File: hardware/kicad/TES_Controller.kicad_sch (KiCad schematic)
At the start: 84 parts, among them CN1 B2PS-VH(LF)(SN), CN2 S4B-XH-A(LF)(SN), CN3 DG381-3.5-02P-14-00A(H), CN5 DG381-3.5-02P-14-00A(H), CN6 DG381-3.5-02P-14-00A(H), Q1 AO3400A, Q2 AO3400A, Q3 AO3400A, Q4 AO3401A, U1 ESP32-S3-WROOM-1-N16R8, U10 DG301-5.0-02P-14-00A(H), U12 TJA1051T/3/1J, U13 24C02S, U5 ADS1115IDGSR, U6 AMS1117-3.3, U8 LMZM23601V5SILR

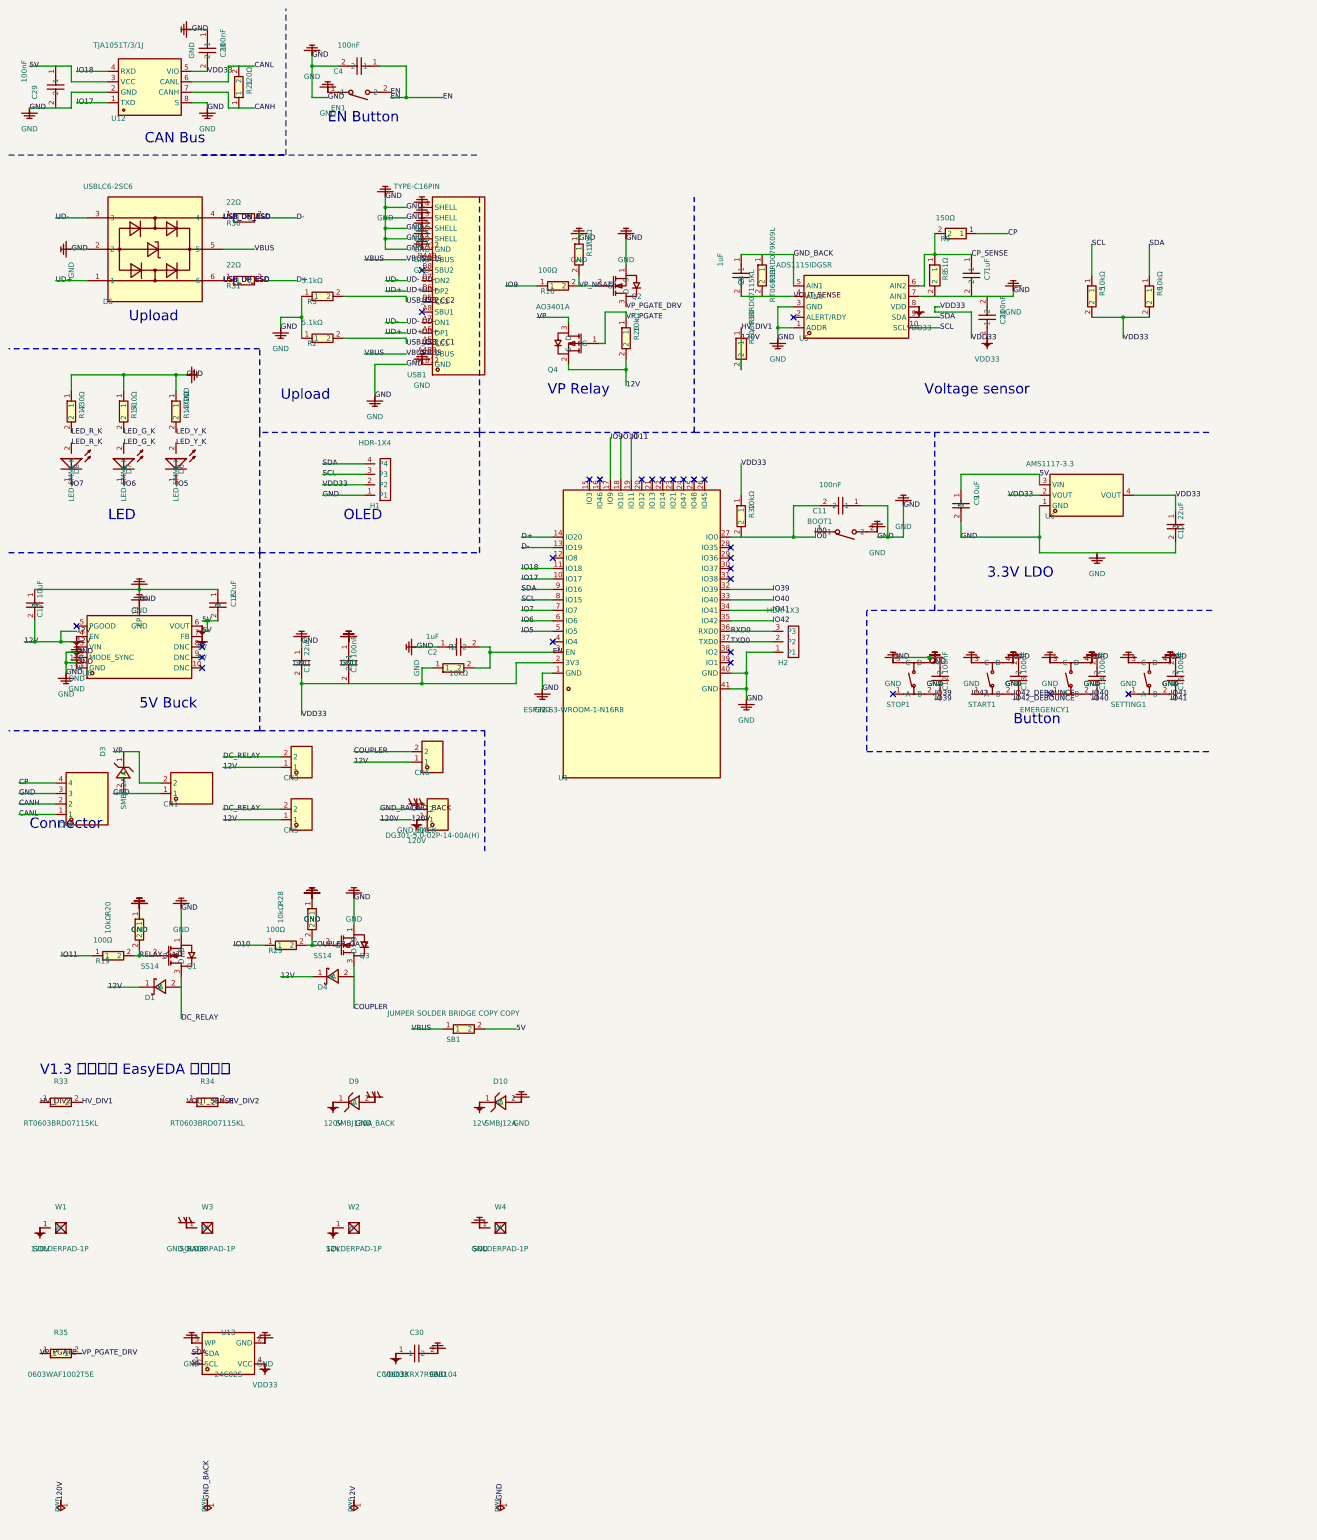
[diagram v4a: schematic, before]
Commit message: Identify the board revision with a divider on ADS1115 AIN3
The U13 EEPROM could not be placed: SDA, SCL and VCC all had to reach it,
and the nearest free spot was 32 mm from the I2C pins. AIN3 was tied to
ground and only served as the CP measurement's negative input, so it now
carries HW_ID from R36/R37 (10k/10k = level 6 = V1.3). Old boards read
0 V and keep the 30.000 coefficient; one net reaches U5 instead of three.

Schematic 236/236 zero difference, ERC 0. PCB hand-routed on the top
layer, DRC 0 errors / 0 unconnected, warnings unchanged at 182,
mechanical lock untouched. R35 and D10 are still to be applied.

Co-Authored-By: Claude Opus 5.5 <noreply@anthropic.com>
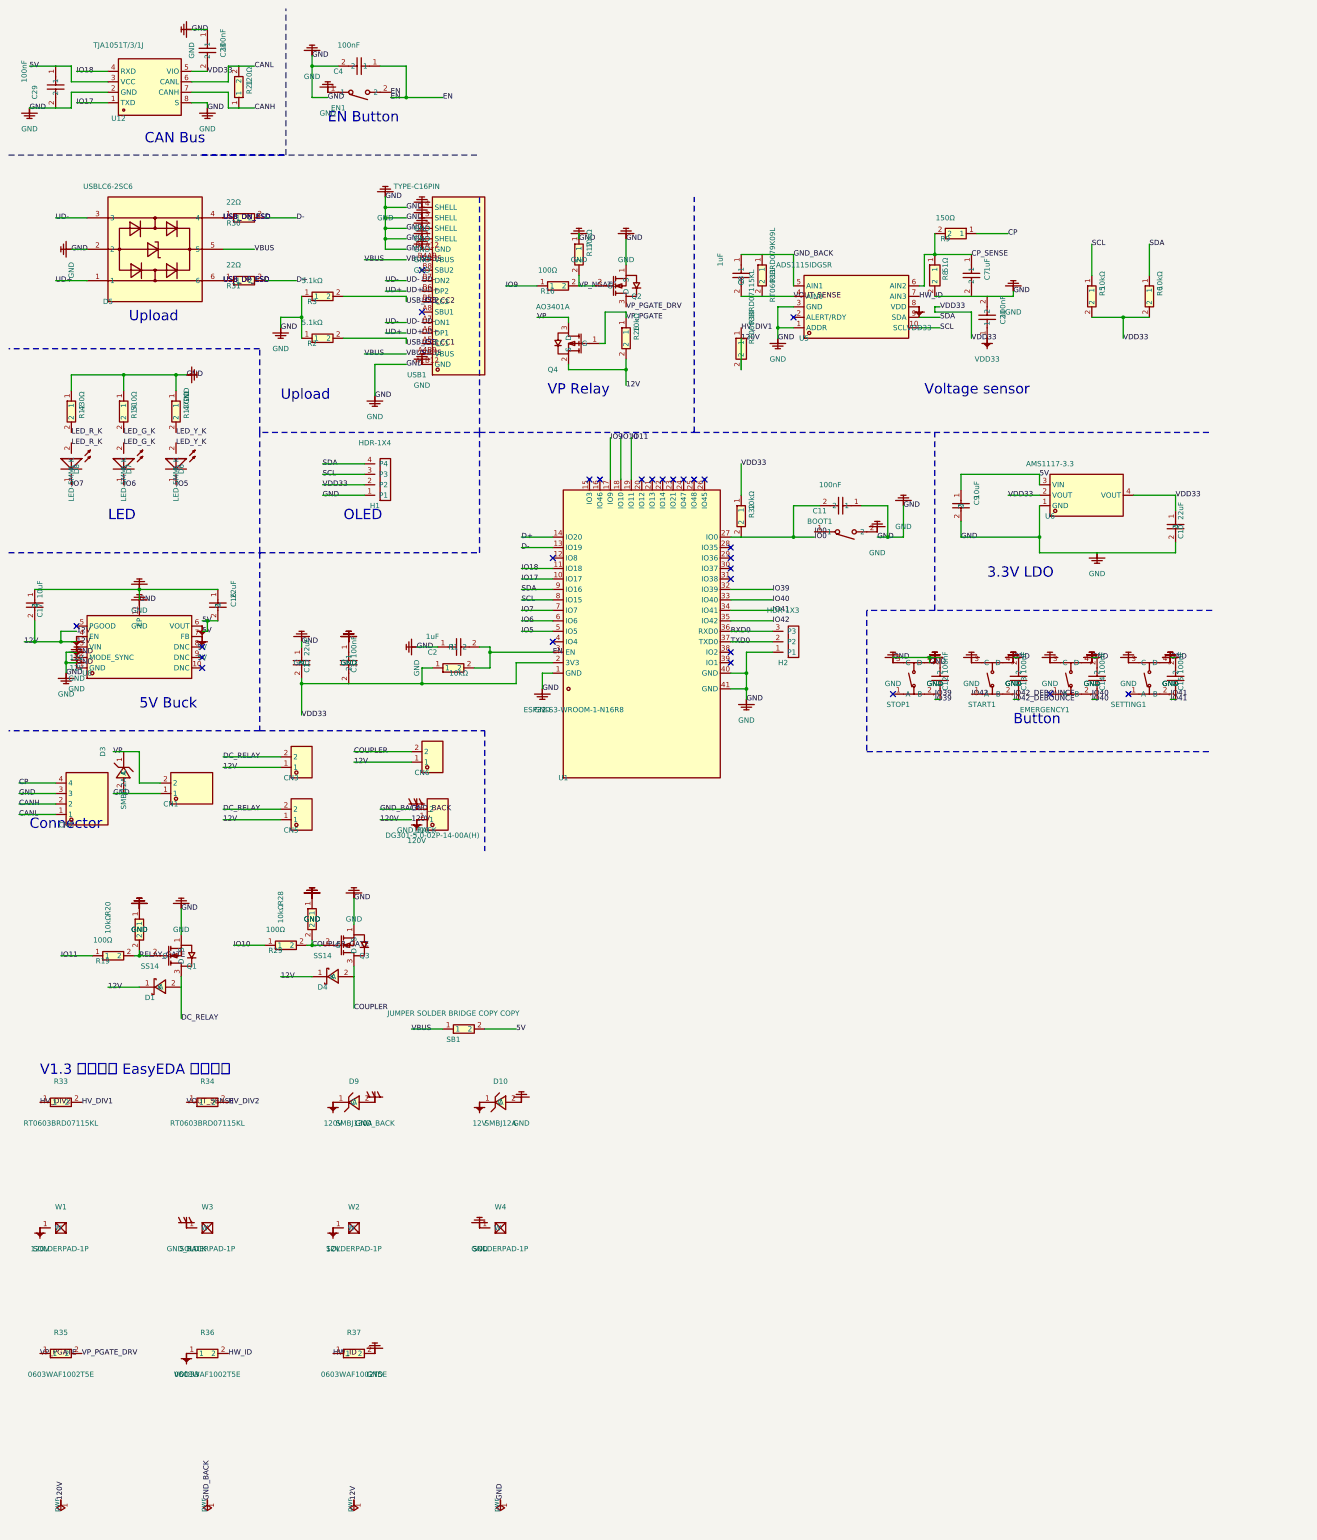
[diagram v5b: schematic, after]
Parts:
- removed C30: CC0603KRX7R9BB104, TES:C0603, symbol TES:CC0603KRX7R9BB104
- removed U13: 24C02S, TES:SOT-23-5_L3.0-W1.6-P0.95-LS2.8-BR, symbol TES:24C02S
- added R36, R37: 0603WAF1002T5E, TES:R0603, symbol TES:0603WAF1002T5E
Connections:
- net GND: now also R37.2; no longer U5.7 (AIN3)
- net VDD33: now also R36.1
- new net HW_ID: R36.2, R37.1, U5.7 (AIN3)

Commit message: Use RT0603BRE07115KL for the 115k divider resistors throughout
The specified RT0603BRD07115KL was down to 2 in stock and the board needs
3. The user accepted the same Yageo RT thin-film part with TCR code E, so
the schematic, the board and the JLCPCB BOM now all carry it instead of
the BOM alone substituting it. JLCPCB's order number is left for their
engineers to place.

Schematic 236/236, ERC 0, DRC 0 errors / 0 unconnected, mechanical check
passes. The regenerated Gerbers differ from the last ones only in date
stamps and aperture-select ordering.

Co-Authored-By: Claude Opus 5.5 <noreply@anthropic.com>
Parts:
- R10, R33, R34: value RT0603BRD07115KL -> RT0603BRE07115KL
